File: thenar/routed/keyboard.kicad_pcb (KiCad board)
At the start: 2 copper layers, 137.3 x 110.9 mm, 99 parts, among them J1 Jumper, J10 Jumper, J11 Jumper, J12 Jumper, J13 Jumper, J14 Jumper, J15 Jumper, J16 Jumper, J17 Jumper, J18 Jumper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

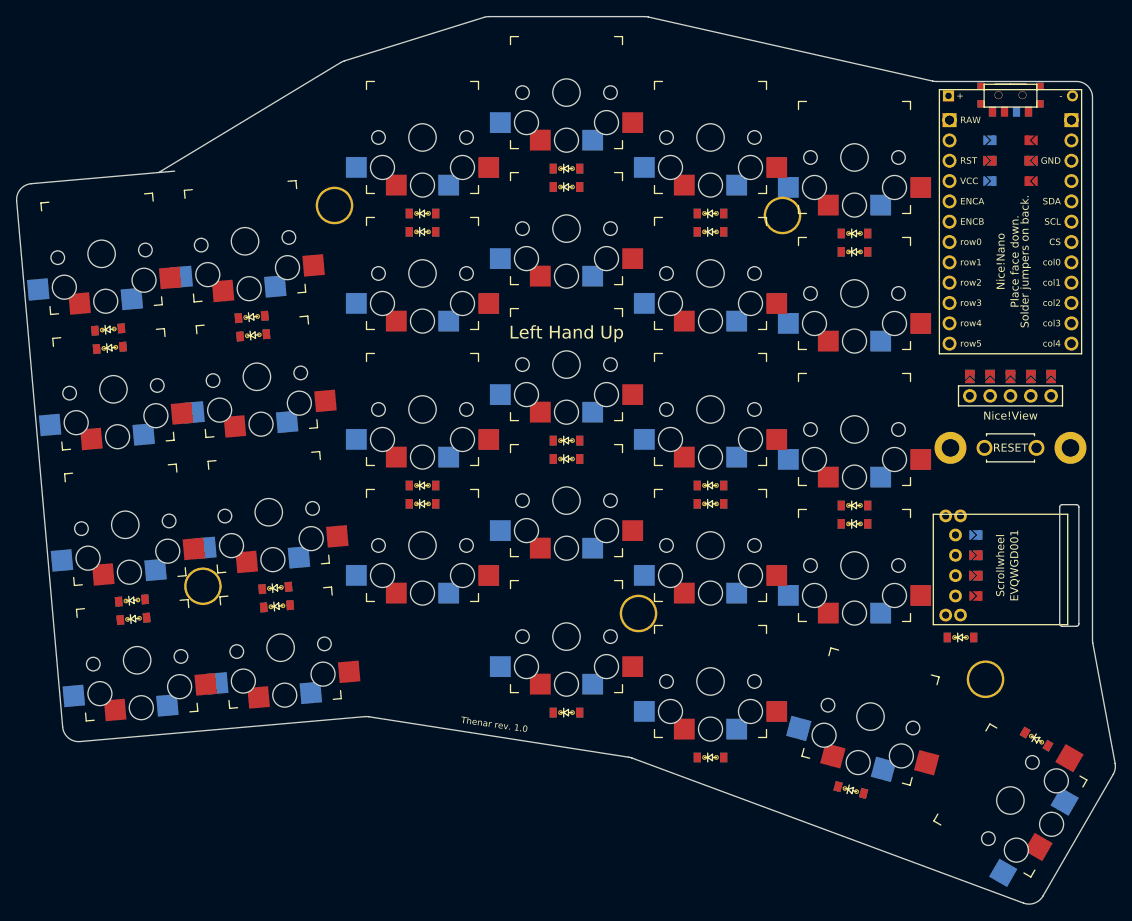
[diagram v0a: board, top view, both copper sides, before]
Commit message: feat(scaffold): auto GND pour + title-block via pcbnew Python
Two pcbnew Python passes wired into the scaffold derivation:

1. Title block populated (Title=Thenar, Company=lytedev, Rev=1.0,
   comments with repo link + description). Previously KiCad showed
   placeholder 'Unknown' and 'keyboard'.

2. F.Cu + B.Cu GND filled zones added covering the board outline. This
   means GND does not need to be hand-routed: every GND-net pad ties
   into the plane automatically. Zones are saved unfilled; gerber export
   passes --check-zones to fill them at fab-output time.

Implementation gotchas that cost a chunk of debugging:

- pcbnew Python segfaults on SaveBoard if the input is KiCad 5.1 format
  (which is what ergogen emits). Solved by running 'kicad-cli pcb
  upgrade' in the scaffold step before invoking pcbnew.
- pcbnew.ZONE.SetOutline takes ownership of a SHAPE_POLY_SET, but Python
  reference counting also wants to free it - double-free crash at save.
  Switched to AppendCorner which copies coordinates instead.
- pcbnew needs a writable HOME for wxConfig. Build derivation sets
  HOME=mktemp -d.

routing.md updated: GND is no longer in the route-by-hand list.
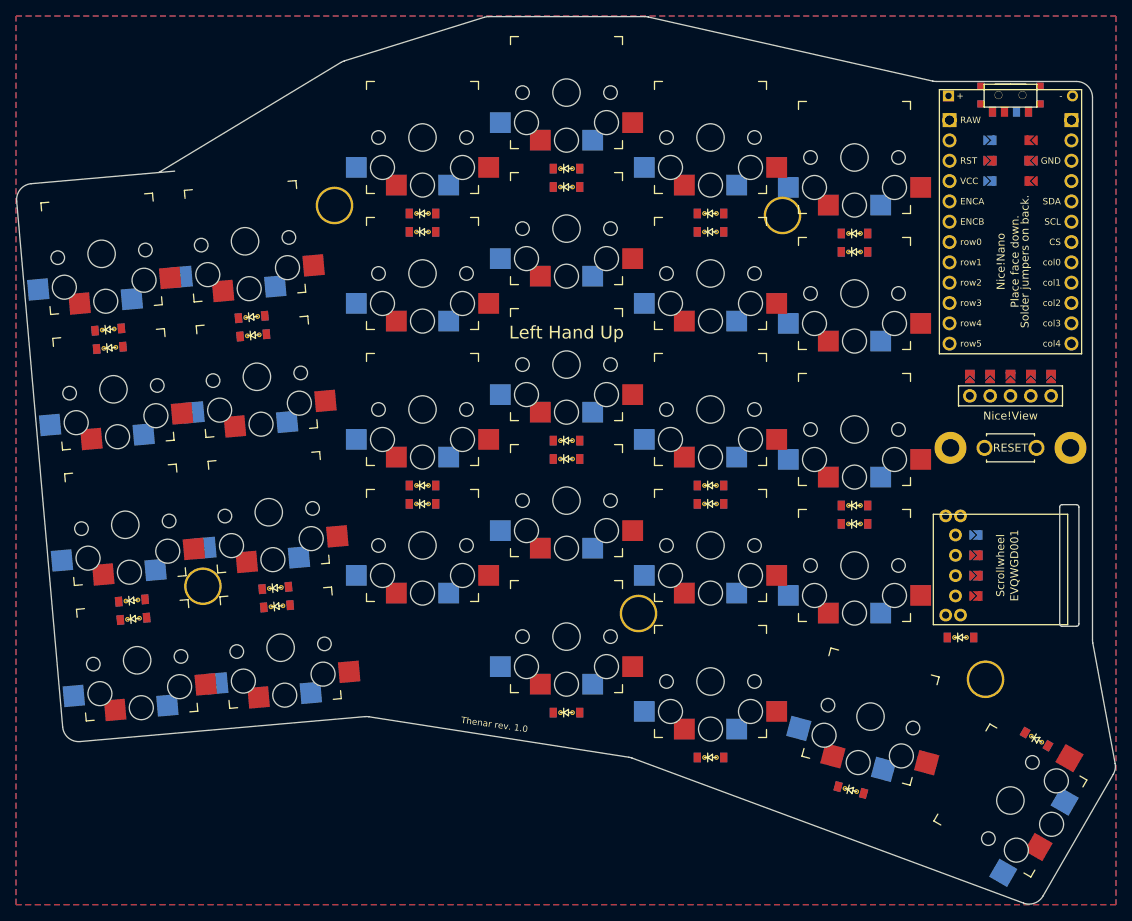
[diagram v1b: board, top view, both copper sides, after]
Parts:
- removed the ? at (115.1, 87.2) (x2)
- removed the ? at (157.1, 148.9)
- removed the ? at (106.1, 136.2) (x2)
- added ? (x2): , lib:text, F.Cu at (115.1, 87.2)
- added ? (x2): , lib:text, F.Cu at (106.1, 136.2)
- added ?: , lib:text, F.Cu at (157.1, 148.9)
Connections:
- MCU1 pad : P1_RAW -> RAW_P1
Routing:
- added copper zone on B.Cu, net GND
- added copper zone on F.Cu, net GND
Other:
- net class Default removed

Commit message: feat(ergogen): close the outline polygon at the outer-num corner
The outline definition added matrix_outer_num top-LEFT followed by top-RIGHT
between outer_top and pinky_num. Because pinky_num top-left is slightly LEFT
of outer_num top-right (pinky column is +1kx, but the polygon shift offsets
collapse the gap to under 2mm), the polygon backtracks at that corner. With
fillet=2 ergogen produces an outline with a non-closing gap there, breaking
DSN export and tripping KiCad's invalid_outline DRC check.

Fix: drop the redundant outer_num top-right point. The polygon now goes
outer_top top-left -> outer_num top-left -> pinky_num top-left, the same
left-edge-then-diagonal shape that worked for the upstream corax. DRC
reports zero invalid_outline violations now.

Also adds a freerouting orchestration script (thenar/scripts/autoroute.py)
that handles the DSN->freerouting->SES roundtrip, but does not wire it
into the flake: the reversible PCB has intentionally-shorted hybrid nets
(NN_GND_SCL etc.) that KiCad's DSN exporter refuses, so the script
currently bails. Docstring documents what a flattening pre-pass would
need to do. routing.md links to this status.

Bumps gitignore: keyboard-drc.rpt and *.kicad_prl (auto-created by KiCad).
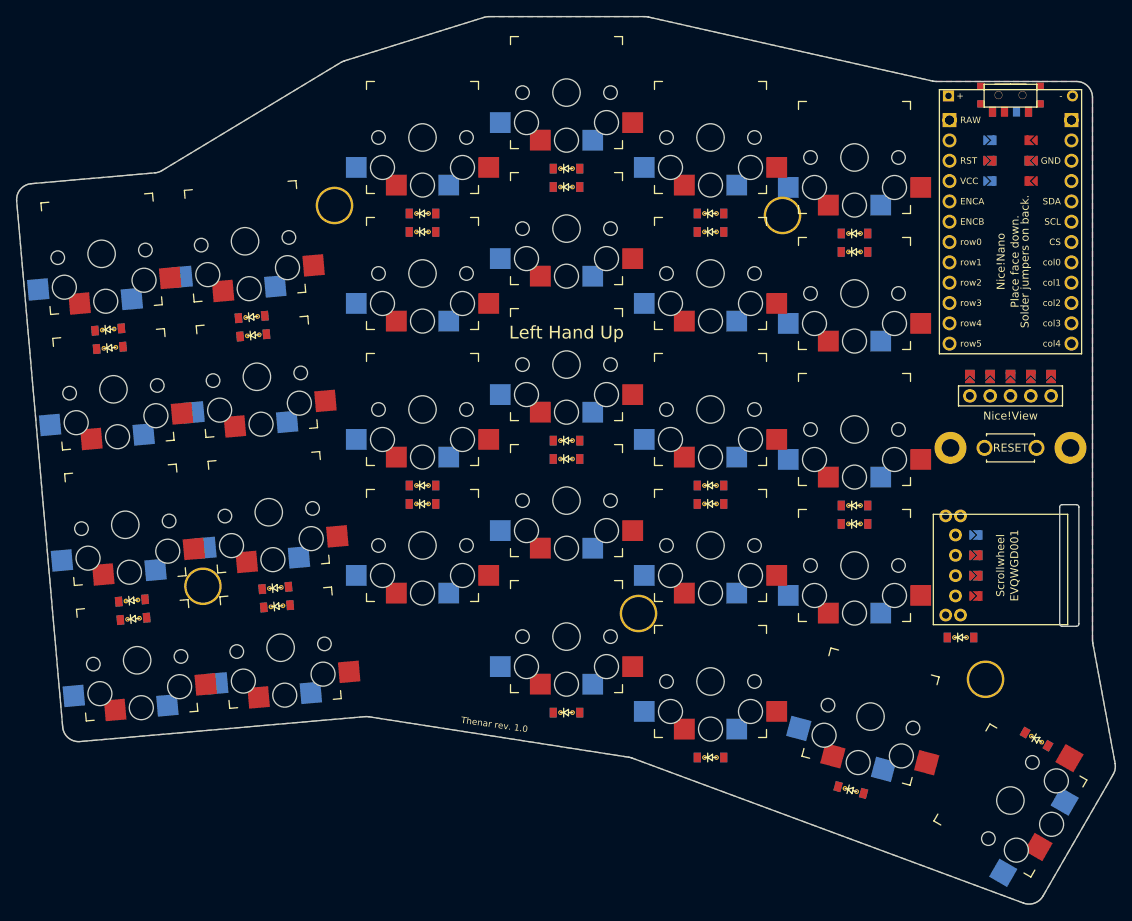
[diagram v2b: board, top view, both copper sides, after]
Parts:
- removed the ? at (115.1, 87.2) (x2)
- removed the ? at (106.1, 136.2) (x2)
- added ? (x2): , lib:text, F.Cu at (106.1, 136.2)
- added ? (x2): , lib:text, F.Cu at (115.1, 87.2)
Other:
- outline, holes or cut-outs redrawn

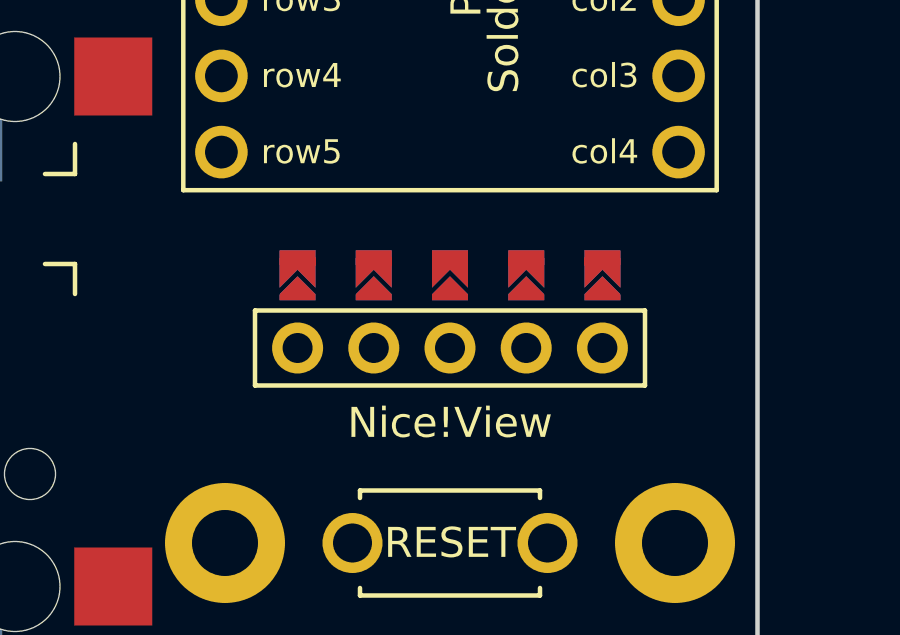
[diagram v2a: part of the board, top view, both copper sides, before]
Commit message: feat(ergogen): migrate Nice!View to ceoloide's single-net-per-pad footprint
The old corax-style niceview.js used the legacy reversible pattern with
two pads numbered '1' on different nets (NN_GND_SCL and NN_CS_SDA), which
KiCad reports as 'two nets shorting on the same pad' and breaks Specctra
DSN export. Replace with ceoloide's display_nice_view (sourced from
github.com/ceoloide/ergogen-footprints), which gives each pin a unique
pad number and generates its own reversibility jumpers as separate SMD
pads.

Config changes:
- Replace 'niceview' (custom) -> 'display_nice_view' (ceoloide)
- Set reversible: true so the footprint emits jumpers
- Drop 10 manual jumper_nv_{left,right}_* entries; ceoloide does this
- Drop 5 NN_* hybrid net names from the niceview pin assignments
- Recompute shift/rotate so the new pads land on the exact same absolute
  spots the old ones occupied (so the existing board outline still fits).
  See thenar/scripts/niceview_placement.py for the solver.

DRC: shorting_items violations: 1 -> 0.
DSN export: still fails (other unknown cause) - this commit makes the
design strictly better but does not yet unblock freerouting.
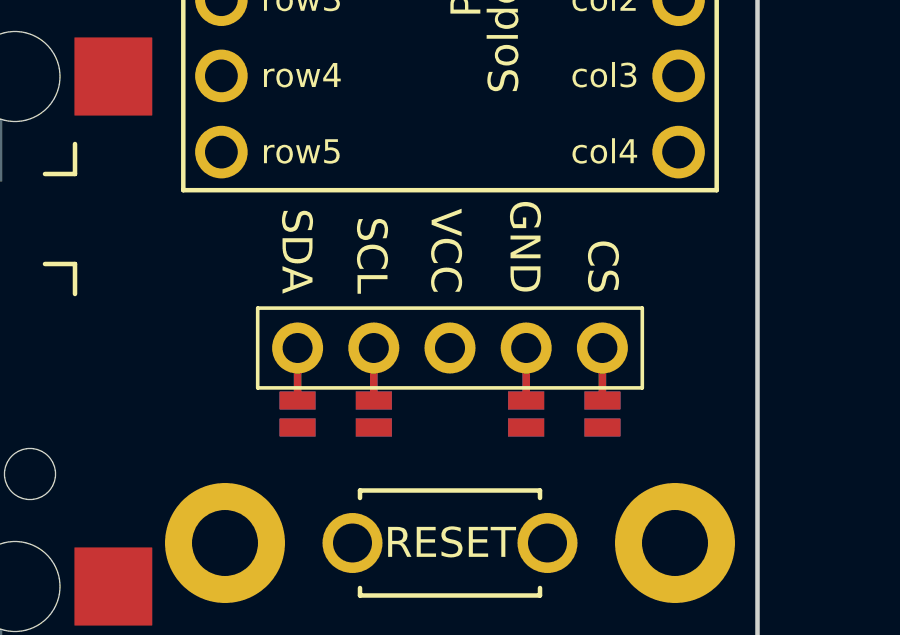
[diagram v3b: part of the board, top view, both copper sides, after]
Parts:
- removed the ? at (106.1, 136.2) (x2)
- removed the ? at (115.1, 87.2) (x2)
- removed J15, J16, J17, J18, J19, J20, J21, J22, J23, J24: Jumper, lib:Jumper
- removed Nice!View1: , lib:niceview_headers
- added ? (x2): , lib:text, F.Cu at (106.1, 136.2)
- added ? (x2): , lib:text, F.Cu at (115.1, 87.2)
- added DISP1: , ceoloide:display_nice_view, F.Cu at (170.6, 111.8)
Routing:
- net DISP1_5: track 0.00 -> 3.50 mm
- net DISP1_4: track 0.00 -> 3.50 mm
- net DISP1_2: track 0.00 -> 3.50 mm
- net DISP1_1: track 0.00 -> 3.50 mm

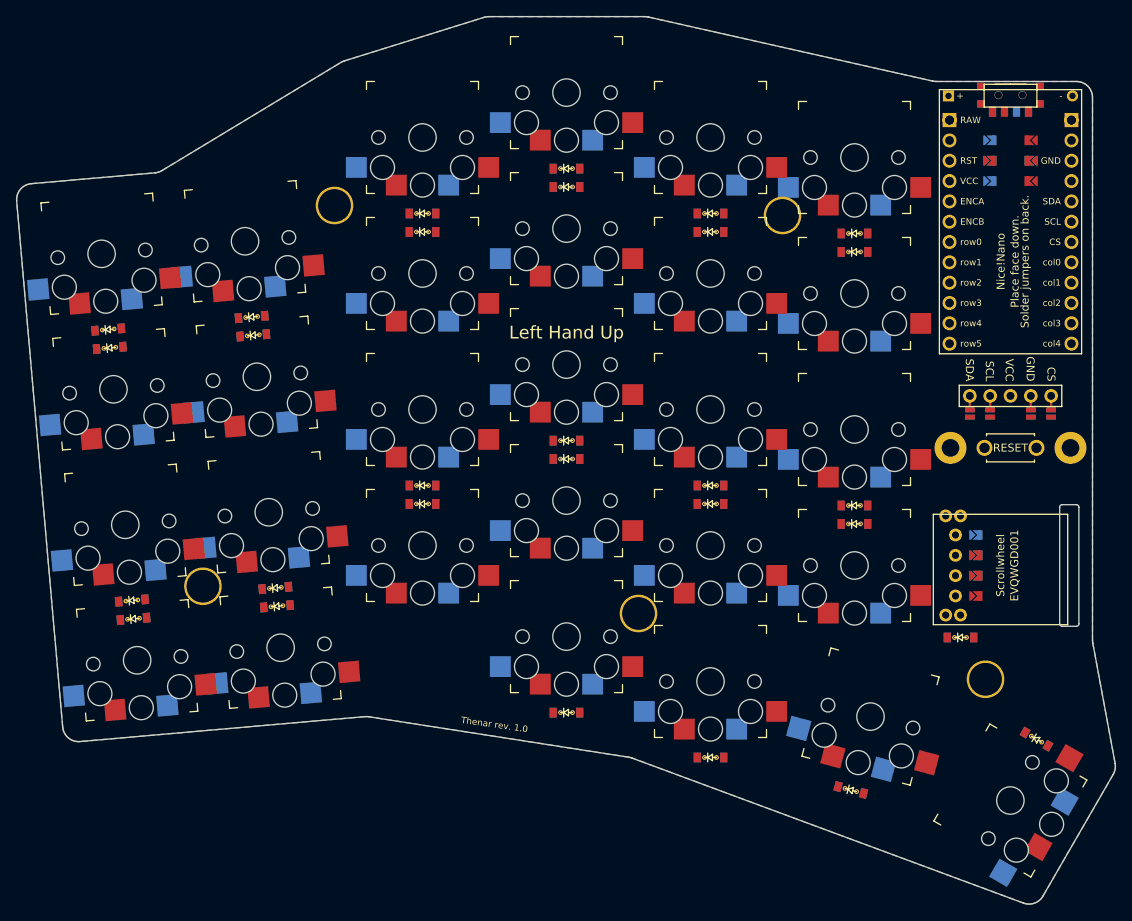
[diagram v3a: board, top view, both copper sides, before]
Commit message: feat(ergogen): migrate Nice!Nano to ceoloide's mcu_nice_nano footprint
Same migration we did for niceview, applied to the MCU. Drop the
external jumper_left_*/jumper_right_* pattern and the hybrid net names
(RAW_P1, RST_GND, VCC_GND, GND_RST, GND_VCC, P1_RAW), and let ceoloide's
footprint generate the reversibility jumpers internally with one net
per pad.

Config: -8 manual jumper entries, -6 hybrid net names, single GND param
instead of GND1/GND2/GND3, single 'reversible: true' flag.

The new footprint's natural orientation is 'tall' (long axis Y) where
ours was 'wide' (long axis X). Compensate with adjust.rotate: 90, which
combined with the mcu anchor's -90 rotation makes the footprint sit
horizontally. The exact pad positions differ from before but everything
still fits within the existing board outline.

Autoroute impact:
- Before: ~12 hybrid jumper items unrouted (RST_GND, RAW_P1, VCC_GND
  and reverses).
- After: those are gone. Same total unrouted count (~35) because some
  matrix-net congestion grew slightly with the new Nice!Nano layout,
  but the unrouted nets are now real-routing problems, not the
  fundamental shared-copper pattern.
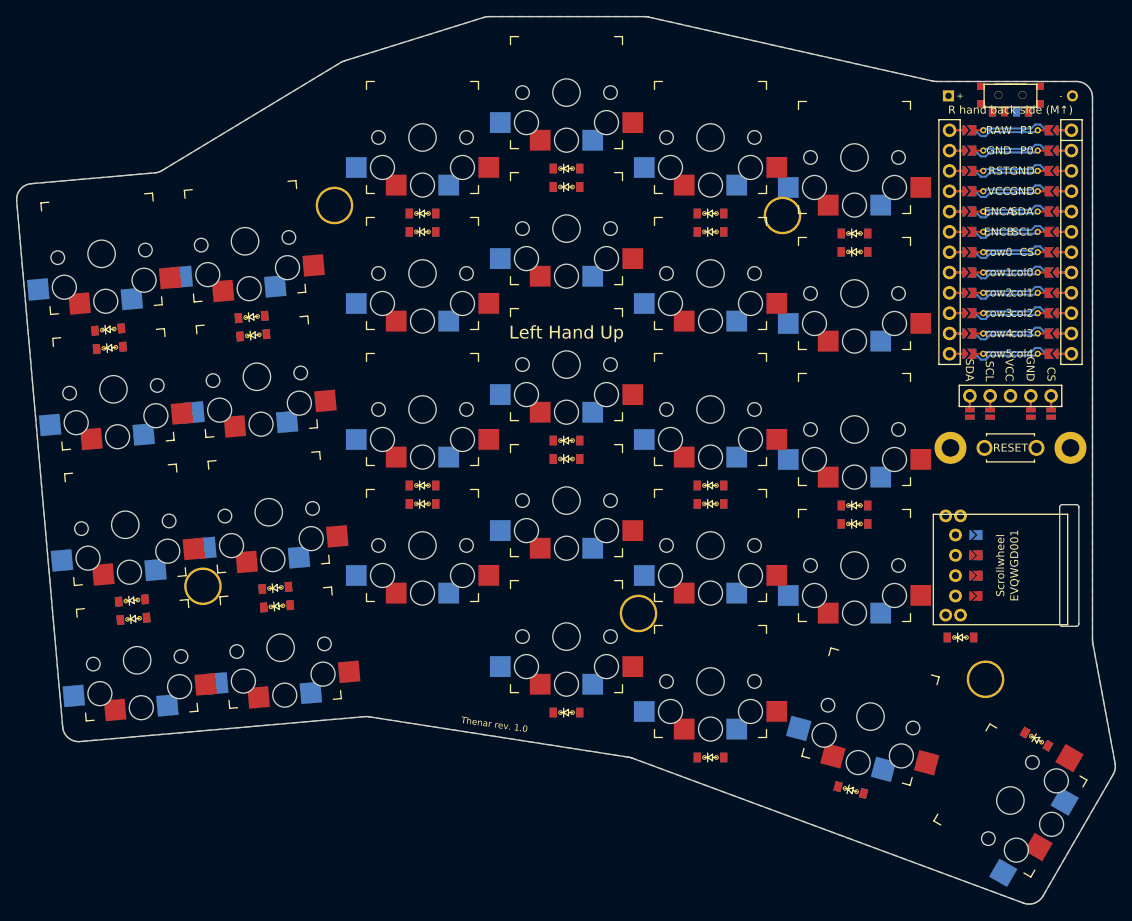
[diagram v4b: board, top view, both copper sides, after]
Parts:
- removed the ? at (106.1, 136.2) (x2)
- removed the ? at (115.1, 87.2) (x2)
- removed J10, J11, J12, J13, J14, J7, J8, J9: Jumper, lib:Jumper
- added ? (x2): , lib:text, F.Cu at (115.1, 87.2)
- added ? (x2): , lib:text, F.Cu at (106.1, 136.2)
- MCU1: footprint ProMicro -> ceoloide:mcu_nice_nano
- turned MCU1 to 0 degrees
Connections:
- net GND_P0 renamed MCU1_2
- net P0_GND renamed MCU1_14
- MCU1 pad 1: RAW_P1 -> MCU1_1
- MCU1 pad 10: row3 -> MCU1_10
- MCU1 pad 11: row4 -> MCU1_11
- MCU1 pad 12: row5 -> MCU1_12
- MCU1 pad 13: P1_RAW -> MCU1_13
- MCU1 pad 15: GND_RST -> MCU1_15
- MCU1 pad 16: GND_VCC -> MCU1_16
- MCU1 pad 17: SDA -> MCU1_17
- MCU1 pad 18: SCL -> MCU1_18
- MCU1 pad 19: CS -> MCU1_19
- MCU1 pad 20: col0 -> MCU1_20
- MCU1 pad 21: col1 -> MCU1_21
- MCU1 pad 22: col2 -> MCU1_22
- MCU1 pad 23: col3 -> MCU1_23
- MCU1 pad 24: col4 -> MCU1_24
- MCU1 pad 3: RST_GND -> MCU1_3
- MCU1 pad 4: VCC_GND -> MCU1_4
- MCU1 pad 5: ENCA -> MCU1_5
- MCU1 pad 6: ENCB -> MCU1_6
- MCU1 pad 7: row0 -> MCU1_7
- MCU1 pad 8: row1 -> MCU1_8
- MCU1 pad 9: row2 -> MCU1_9
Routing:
- net GND: track 0.00 -> 29.5 mm
- net VCC: track 0.00 -> 9.84 mm
- net ENCB: track 0.00 -> 9.84 mm
- net row1: track 0.00 -> 9.84 mm
- net row4: track 0.00 -> 9.84 mm
- net RAW: track 0.00 -> 9.84 mm
- net row5: track 0.00 -> 9.84 mm
- net row3: track 0.00 -> 9.84 mm
- net row0: track 0.00 -> 9.84 mm
- net RST: track 0.00 -> 9.84 mm
- net ENCA: track 0.00 -> 9.84 mm
- net row2: track 0.00 -> 9.84 mm
- net col1: track 0.00 -> 9.83 mm
- net SDA: track 0.00 -> 9.83 mm
- net P0: track 0.00 -> 9.83 mm
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
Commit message: feat(ergogen): give scrollwheel pads unique local nets
The encoder pads A/B/C/D were assigned hybrid net names (ENCB_undef,
GND_ENCA, ENCA_GND, undef_ENCB) - one piece of copper carrying two
different signals depending on which side of the reversible PCB the
encoder is mounted on. Freerouting can't autoroute these because the
'net' identity is ambiguous.

Same fix pattern as the Nice!Nano migration, but at the config level
(no footprint change needed): each encoder pad gets a UNIQUE local
net (sw_a, sw_b, sw_c, sw_d) with one routing endpoint, and the
existing jumper bridge between real signals (ENCA/ENCB/GND) and the
local nets handles the per-side selection.

Renaming for clarity:
  jumper_sw_left_a    -> jumper_sw_left_encb   (clearer about what it does)
  jumper_sw_right_a   -> jumper_sw_right_encb
  jumper_sw_*_ENCA    -> jumper_sw_*_enca      (kebab consistency)

Autoroute impact: ENCB_undef, undef_ENCB, ENCA_GND, GND_ENCA - all four
hybrid-jumper nets are eliminated. Unrouted count went from ~35 -> 31.
The remaining unrouted nets are now all genuine routing congestion
(matrix cols/rows, short hops between encoder pads and their jumpers
that more freerouting passes should resolve).
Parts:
- removed the ? at (115.1, 87.2) (x2)
- removed the ? at (106.1, 136.2) (x2)
- added ? (x2): , lib:text, F.Cu at (115.1, 87.2)
- added ? (x2): , lib:text, F.Cu at (106.1, 136.2)
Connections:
- net ENCA_GND renamed sw_c
- net ENCB_undef renamed sw_a
- net GND_ENCA renamed sw_b
- net undef_ENCB renamed sw_d
